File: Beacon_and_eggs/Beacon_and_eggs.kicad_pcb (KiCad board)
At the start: 2 copper layers, 47.7 x 65.9 mm, 42 parts, among them J1 USB_C_Receptacle_USB2.0_16P, Q1 IRLML0030, SW1 Boot, SW2 Reset, U1 SA818V, U2 STM32F411CEUx, U3 ADXL343, U6 MCP1253-33X50I/MS, U7 MCP1253-33X50I/MS, Y1 25MHz 18pF, Y2 32.768kHz 12.5pF

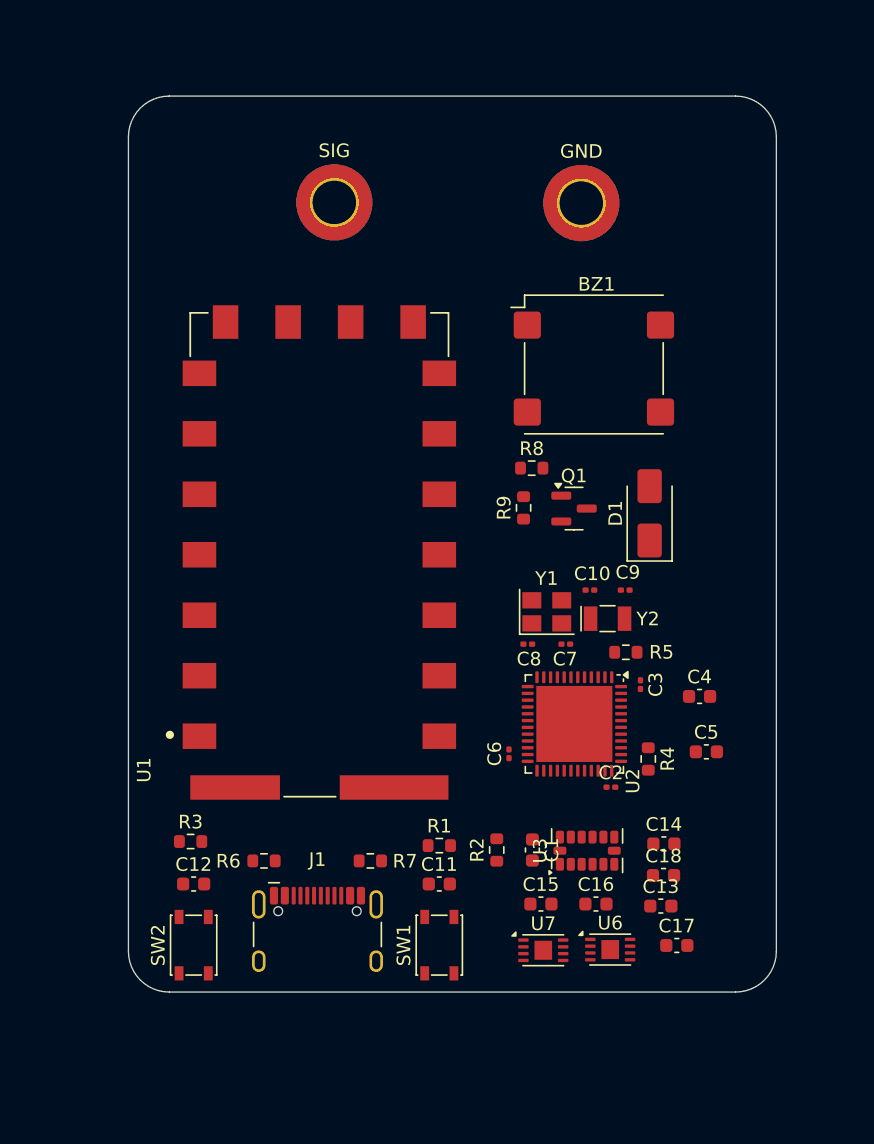
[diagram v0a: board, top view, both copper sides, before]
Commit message: Laid traces and changed 3.3V regulator
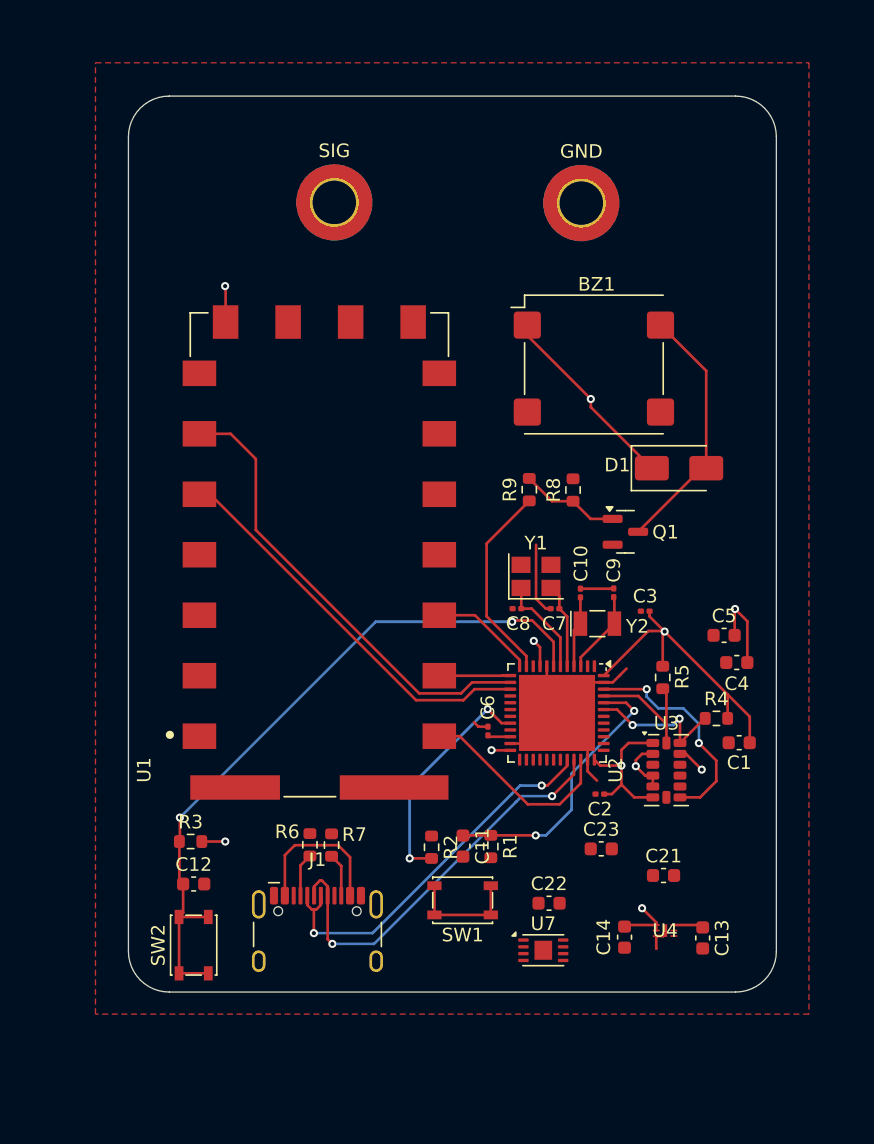
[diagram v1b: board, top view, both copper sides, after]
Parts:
- removed C15: 10uF, Capacitor_SMD:C_0603_1608Metric
- removed U6: MCP1253-33X50I/MS, Package_DFN_QFN:TDFN-8-1EP_3x2mm_P0.5mm_EP1.3x1.4mm
- added U4: MIC5528-3.3YMX-TR, footprints:XTDFN6_1P2X1P2_MCH, F.Cu at (156.9, 116.3)
- C14: value 1uF -> 2.2uF
- moved C1 17.1 mm to (162.4, 102.5), turned to 0 degrees
- moved C23 9.03 mm to (152.2, 110.3)
- moved C5 8.67 mm to (161.3, 94.6), turned to 180 degrees
- moved U3 8.32 mm to (157.0, 104.5), turned to 0 degrees
- moved C14 7.45 mm to (153.9, 116.8), turned to -90 degrees
- moved R4 5.84 mm to (160.7, 100.7), turned to 0 degrees
- moved C3 5.42 mm to (155.4, 92.8), turned to 180 degrees
- moved R2 4.80 mm to (139.7, 110.2), turned to -90 degrees
- moved Q1 4.15 mm to (154.0, 87.0)
- moved D1 3.96 mm to (157.9, 82.3), turned to 0 degrees
- moved C13 3.87 mm to (159.7, 116.9), turned to -90 degrees
- moved R1 3.79 mm to (144.1, 110.2), turned to -90 degrees
- moved SW1 3.72 mm to (142.0, 114.1), turned to 0 degrees
- moved C4 3.71 mm to (162.2, 96.6)
- moved R6 3.58 mm to (130.8, 110.0), turned to 90 degrees
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- renumbered C18 to C21, C16 to C22, C17 to C23
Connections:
- C14 pad 1: Net-(U6-C+) -> +3.3V
- C14 pad 2: Net-(U6-C-) -> GND
- J1 pad A4: +3.3V -> +5V
- J1 pad A9: +3.3V -> +5V
- J1 pad B4: +3.3V -> +5V
- J1 pad B9: +3.3V -> +5V
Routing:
- net +3.3V: track 0.00 -> 81.0 mm, vias 0 -> 10
- net NRST: track 0.00 -> 51.8 mm, vias 0 -> 2
- net GND: track 0.00 -> 36.1 mm, vias 0 -> 1
- net TX POWER DOWN: track 0.00 -> 34.2 mm
- net USB Dp: track 0.00 -> 30.4 mm, vias 0 -> 2
- net TX EN: track 0.00 -> 29.5 mm
- net USB Dn: track 0.00 -> 28.6 mm, vias 0 -> 2
- net BOOT0: track 0.00 -> 20.5 mm, vias 0 -> 2
- net Net-(BZ1--): track 0.00 -> 18.9 mm
- net BOOT1: track 0.00 -> 17.1 mm, vias 0 -> 2
- net ACCEL INT1: track 0.00 -> 16.3 mm, vias 0 -> 2
- net TX AUDIO SIGNAL: track 0.00 -> 14.9 mm
- net BUZZ: track 0.00 -> 14.7 mm
- net +5V: track 0.00 -> 11.3 mm
- net SDA: track 0.00 -> 10.7 mm, vias 0 -> 2
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- added copper zone on In1.Cu, net +3.3V
- added copper zone on F.Cu, net GND
- added copper zone on In2.Cu, net GND
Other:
- copper layers 2 -> 4

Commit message: cheanged schematic and V1 pcb layout completed.
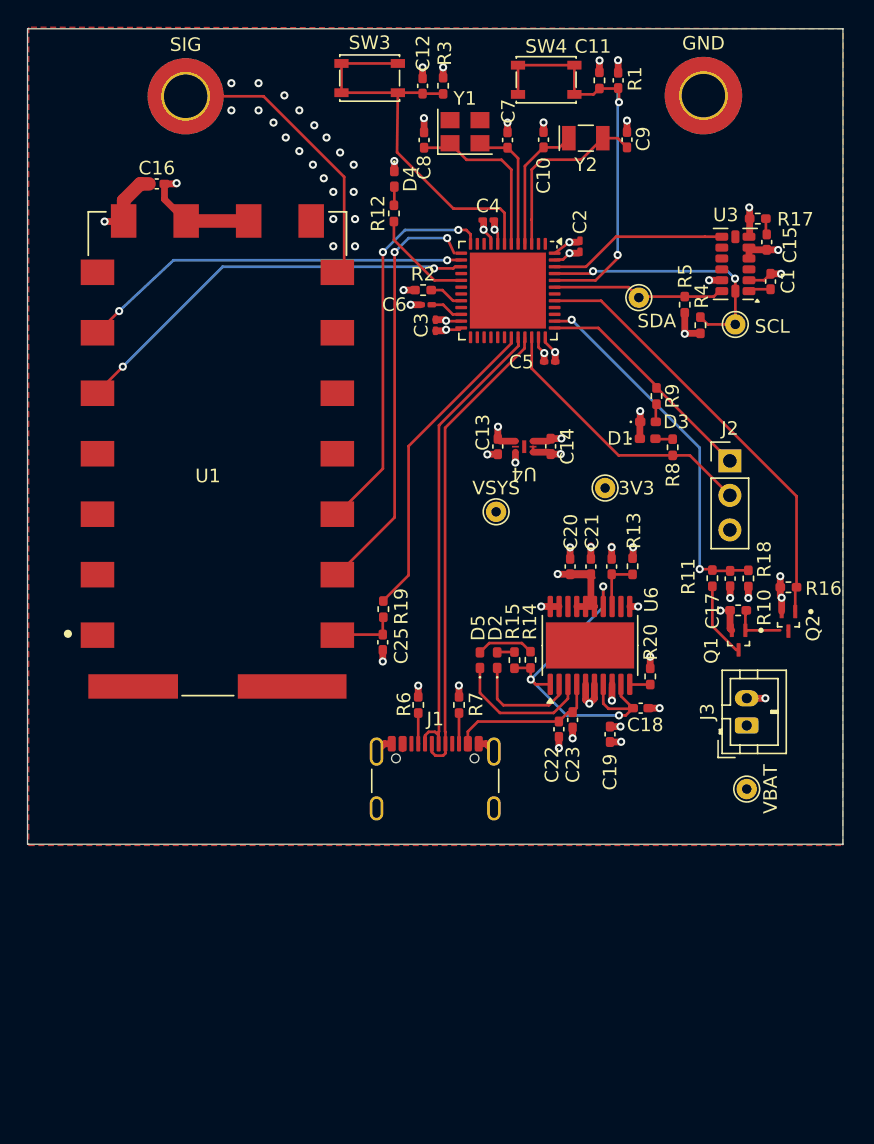
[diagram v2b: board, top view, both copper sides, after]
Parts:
- removed BZ1: Buzzer, Buzzer_Beeper:MagneticBuzzer_PUI_SMT-1028-T-2-R
- removed the GND at (150.8, 62.8)
- removed SW1: Boot, Button_Switch_SMD:SW_SPST_PTS810
- removed SW2: Reset, Button_Switch_SMD:SW_SPST_PTS810
- removed U7: MCP1253-33X50I/MS, Package_DFN_QFN:TDFN-8-1EP_3x2mm_P0.5mm_EP1.3x1.4mm
- added 3V3: 3V3, TestPoint:TestPoint_THTPad_D1.5mm_Drill0.7mm, F.Cu at (152.5, 83.8)
- added C15: 10uF, Capacitor_SMD:C_0402_1005Metric_Pad0.74x0.62mm_HandSolder, F.Cu at (164.4, 65.7)
- added C16: 0.1uF, Capacitor_SMD:C_0402_1005Metric_Pad0.74x0.62mm_HandSolder, F.Cu at (119.5, 61.4)
- added C17: 1nF, Capacitor_SMD:C_0402_1005Metric_Pad0.74x0.62mm_HandSolder, F.Cu at (161.7, 90.5)
- added C18: 0.1uF, Capacitor_SMD:C_0402_1005Metric_Pad0.74x0.62mm_HandSolder, F.Cu at (155.1, 100.0)
- added C19: 33uF, Capacitor_SMD:C_0402_1005Metric_Pad0.74x0.62mm_HandSolder, F.Cu at (152.9, 101.9)
- added C20: 0.1uF, Capacitor_SMD:C_0402_1005Metric_Pad0.74x0.62mm_HandSolder, F.Cu at (149.9, 89.6)
- added C24: 10nF, Capacitor_SMD:C_0402_1005Metric_Pad0.74x0.62mm_HandSolder, F.Cu at (153.0, 89.6)
- added C25: 33nF, Capacitor_SMD:C_0402_1005Metric_Pad0.74x0.62mm_HandSolder, F.Cu at (136.1, 95.1)
- added D2: RED LED, LED_SMD:LED_0402_1005Metric_Pad0.77x0.64mm_HandSolder, F.Cu at (144.6, 96.5)
- added D3: UCLAMP3311P.TCT, Diode_SMD:D_0402_1005Metric_Pad0.77x0.64mm_HandSolder, F.Cu at (155.7, 78.9)
- added D4: BLUE LED, LED_SMD:LED_0402_1005Metric_Pad0.77x0.64mm_HandSolder, F.Cu at (137.0, 61.0)
- added D5: GREEN LED, LED_SMD:LED_0402_1005Metric_Pad0.77x0.64mm_HandSolder, F.Cu at (143.3, 96.5)
- added GND: MountingHole_3.2mm_M3_ISO7380_Pad_TopBottom, MountingHole:MountingHole_3.2mm_M3_ISO7380_Pad_TopBottom, F.Cu at (159.7, 54.9)
- added J2: Conn_01x03_Pin, Connector_PinHeader_2.54mm:PinHeader_1x03_P2.54mm_Vertical, F.Cu at (161.7, 81.8)
- added J3: Conn_01x02_Pin, Connector_JST:JST_PH_B2B-PH-K_1x02_P2.00mm_Vertical, F.Cu at (162.9, 101.3)
- added Q2: NTA4153N, NTA4151PT1G:SOT50P160X90-3N, F.Cu at (166.0, 93.6)
- added R10: 51k, Resistor_SMD:R_0402_1005Metric_Pad0.72x0.64mm_HandSolder, F.Cu at (162.3, 92.8)
- added R11: 51k, Resistor_SMD:R_0402_1005Metric_Pad0.72x0.64mm_HandSolder, F.Cu at (160.4, 90.4)
- added R12: 250R, Resistor_SMD:R_0402_1005Metric_Pad0.72x0.64mm_HandSolder, F.Cu at (137.0, 63.6)
- added R13: 37.4K, Resistor_SMD:R_0402_1005Metric_Pad0.72x0.64mm_HandSolder, F.Cu at (154.5, 89.5)
- added R14: 1.5K, Resistor_SMD:R_0402_1005Metric_Pad0.72x0.64mm_HandSolder, F.Cu at (147.0, 96.4)
- added R15: 1.5K, Resistor_SMD:R_0402_1005Metric_Pad0.72x0.64mm_HandSolder, F.Cu at (145.8, 96.5)
- added R16: 510k, Resistor_SMD:R_0402_1005Metric_Pad0.72x0.64mm_HandSolder, F.Cu at (166.0, 91.1)
- added R17: 50R, Resistor_SMD:R_0402_1005Metric_Pad0.72x0.64mm_HandSolder, F.Cu at (163.7, 64.0)
- added R18: 51k, Resistor_SMD:R_0402_1005Metric_Pad0.72x0.64mm_HandSolder, F.Cu at (163.0, 90.4)
- added R19: 3.3K, Resistor_SMD:R_0402_1005Metric_Pad0.72x0.64mm_HandSolder, F.Cu at (136.2, 92.7)
- added R20: 1K, Resistor_SMD:R_0402_1005Metric_Pad0.72x0.64mm_HandSolder, F.Cu at (155.8, 97.7)
- added SW3: RESET, Button_Switch_SMD:SW_SPST_PTS810, F.Cu at (135.2, 53.6)
- added SW4: BOOT0, Button_Switch_SMD:SW_SPST_PTS810, F.Cu at (148.2, 53.8)
- added TP3: SCL, TestPoint:TestPoint_THTPad_D1.5mm_Drill0.7mm, F.Cu at (162.1, 71.8)
- added TP4: SDA, TestPoint:TestPoint_THTPad_D1.5mm_Drill0.7mm, F.Cu at (155.0, 69.8)
- added TP5: VBAT, TestPoint:TestPoint_THTPad_D1.5mm_Drill0.7mm, F.Cu at (162.9, 105.9)
- added TP6: VSYS, TestPoint:TestPoint_THTPad_D1.5mm_Drill0.7mm, F.Cu at (144.5, 85.5)
- added U6: BQ24070RHLR, Package_SO:HTSSOP-20-1EP_4.4x6.5mm_P0.65mm_EP3.4x6.5mm_Mask2.4x3.7mm, F.Cu at (151.4, 95.4)
- C1: value C -> 0.1F; footprint Capacitor_SMD:C_0603_1608Metric -> Capacitor_SMD:C_0402_1005Metric_Pad0.74x0.62mm_HandSolder
- C10, C7, C8, C9: footprint Capacitor_SMD:C_0201_0603Metric -> Capacitor_SMD:C_0402_1005Metric_Pad0.74x0.62mm_HandSolder
- C11, C12, C14, C21: footprint Capacitor_SMD:C_0603_1608Metric -> Capacitor_SMD:C_0402_1005Metric_Pad0.74x0.62mm_HandSolder
- C13: value 10uF -> 2.2uF; footprint Capacitor_SMD:C_0603_1608Metric -> Capacitor_SMD:C_0402_1005Metric_Pad0.74x0.62mm_HandSolder
- C2, C3, C6: footprint Capacitor_SMD:C_0201_0603Metric -> Capacitor_SMD:C_0201_0603Metric_Pad0.64x0.40mm_HandSolder
- C22: value 10uF -> 0.1uF; footprint Capacitor_SMD:C_0603_1608Metric -> Capacitor_SMD:C_0402_1005Metric_Pad0.74x0.62mm_HandSolder
- C23: value 1uF -> 10uF; footprint Capacitor_SMD:C_0603_1608Metric -> Capacitor_SMD:C_0402_1005Metric_Pad0.74x0.62mm_HandSolder
- C4, C5: footprint Capacitor_SMD:C_0603_1608Metric -> Capacitor_SMD:C_0201_0603Metric_Pad0.64x0.40mm_HandSolder
- D1: value SS14 -> UCLAMP3311P.TCT; footprint Diode_SMD:D_SMA -> Diode_SMD:D_0402_1005Metric_Pad0.77x0.64mm_HandSolder
- J1: footprint Connector_USB:USB_C_Receptacle_HCTL_HC-TYPE-C-16P-01A -> Connector_USB:USB_C_Receptacle_GCT_USB4105-xx-A_16P_TopMnt_Horizontal
- Q1: value IRLML0030 -> NTA4151P; footprint Package_TO_SOT_SMD:SOT-23 -> NTA4151PT1G:SOT50P160X90-3N
- R1, R2, R3, R4, R5, R6, R7: footprint Resistor_SMD:R_0603_1608Metric -> Resistor_SMD:R_0402_1005Metric_Pad0.72x0.64mm_HandSolder
- R8: value 100k -> 250R; footprint Resistor_SMD:R_0603_1608Metric -> Resistor_SMD:R_0402_1005Metric_Pad0.72x0.64mm_HandSolder
- R9: value 100 -> 250R; footprint Resistor_SMD:R_0603_1608Metric -> Resistor_SMD:R_0402_1005Metric_Pad0.72x0.64mm_HandSolder
- SIG: value MountingHole_3.2mm_M3_DIN965_Pad_TopBottom -> FABRIC_ANT_HOLES
- moved C12 61.1 mm to (139.1, 54.2), turned to 90 degrees
- moved R3 58.6 mm to (140.6, 54.2), turned to 90 degrees
- moved C11 57.5 mm to (153.5, 53.8), turned to 90 degrees
- moved R1 56.9 mm to (152.1, 53.8)
- moved R2 41.0 mm to (139.1, 69.2), turned to 0 degrees
- moved C2 40.3 mm to (150.7, 66.0), turned to 90 degrees
- moved C13 39.2 mm to (144.6, 80.7)
- moved U3 37.6 mm to (162.1, 67.3), turned to 180 degrees
- moved C4 37.3 mm to (143.9, 64.1), turned to 180 degrees
- moved U4 37.1 mm to (146.5, 80.7), turned to 180 degrees
- moved C14 36.5 mm to (148.5, 80.7), turned to 90 degrees
- moved Y2 35.7 mm to (151.1, 58.0)
- moved C8 35.2 mm to (139.2, 58.2), turned to -90 degrees
- moved C7 34.7 mm to (145.3, 58.2), turned to -90 degrees
- moved C1 34.0 mm to (164.7, 68.6), turned to 90 degrees
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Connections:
- net ACCEL INT1 renamed /ACCEL_INT1
- net BOOT1 renamed /BOOT1
- net NRST renamed /NRST
- net Net-(U2-PC14) renamed /X2_IN
- net Net-(U2-PC15) renamed /X2_OUT
- net Net-(U2-PH0) renamed /X1_IN
- net Net-(U2-PH1) renamed /X1_OUT
- net RXD renamed /RXD
- net TX EN renamed /TX_EN
- net TX POWER DOWN renamed /TX_PWR_DN
- net TXD renamed /TXD
- net USB Dn renamed /USB_DN
- net USB Dp renamed /USB_DP
- C1 pad 1: GND -> Net-(U3-Vdd_I/O)
- C1 pad 2: +3.3V -> GND
- C11 pad 1: BOOT0 -> /BOOT0
- C13 pad 1: +BATT -> VSYS
- C21 pad 1: +5V -> VSYS
- C22 pad 1: +3V3 -> VBUS
- C23 pad 1: Net-(U7-C+) -> VBUS
- C23 pad 2: Net-(U7-C-) -> GND
- D1 pad 1: +3.3V -> GND
- D1 pad 2: Net-(BZ1--) -> Net-(D1-A2)
- J1 pad A4: +5V -> VBUS
- J1 pad A9: +5V -> VBUS
- J1 pad B4: +5V -> VBUS
- J1 pad B9: +5V -> VBUS
- Q1 pad 1: Net-(Q1-G) -> Net-(Q1-G1)
- Q1 pad 2: GND -> VBAT
- Q1 pad 3: Net-(BZ1--) -> Net-(Q1-D1-Pad3)
- R1 pad 1: BOOT0 -> GND
- R1 pad 2: GND -> /BOOT0
- R4 pad 1: SDA -> /SCL
- R5 pad 1: SCL -> /SDA
- R8 pad 1: Net-(Q1-G) -> Net-(D1-A2)
- R8 pad 2: GND -> /SWDIO
- R9 pad 1: BUZZ -> /SWCLK
- R9 pad 2: Net-(Q1-G) -> Net-(D3-A2)
- SIG pad 1: (no net) -> /ANT_SIG
- U1 pad 12: RF_IN -> /ANT_SIG
- U1 pad 18: TX AUDIO SIGNAL -> Net-(U1-MIC_IN)
- U1 pad 8: +3.3V -> VSYS
- U2 pad 11: BUZZ -> unconnected-(U2-PA1-Pad11)
- U2 pad 17: unconnected-(U2-PA7-Pad17) -> /LED1
- U2 pad 29: REG_SHDN -> unconnected-(U2-PA8-Pad29)
- U2 pad 31: unconnected-(U2-PA10-Pad31) -> /TX_AUDIO_SIGNAL
- U2 pad 34: TX AUDIO SIGNAL -> /SWDIO
- U2 pad 37: unconnected-(U2-PA14-Pad37) -> /SWCLK
- U2 pad 38: unconnected-(U2-PA15-Pad38) -> /BATT_V_ADC
- U2 pad 41: unconnected-(U2-PB5-Pad41) -> /BATT_EN
- U2 pad 43: SDA -> /SDA
- U2 pad 44: BOOT0 -> /BOOT0
- U2 pad 45: SCL -> /SCL
- U3 pad 1: +3.3V -> Net-(U3-Vdd_I/O)
- U3 pad 13: SDA -> /SDA
- U3 pad 14: SCL -> /SCL
- U4 pad 4: unconnected-(U4-EN-Pad4) -> VSYS
- U4 pad 6: +BATT -> VSYS
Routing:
- net +3.3V: track 81.0 -> 17.4 mm, vias 10 -> 9
- net /BATT_EN: track 0.00 -> 32.4 mm
- net /BOOT0: track 0.00 -> 30.9 mm, vias 0 -> 2
- net /VREF: track 0.00 -> 28.9 mm, vias 0 -> 3
- net /BATT_V_ADC: track 0.00 -> 27.2 mm, vias 0 -> 2
- net /TXD: track 6.36 -> 31.0 mm, vias 0 -> 2
- net /TX_AUDIO_SIGNAL: track 0.00 -> 23.3 mm
- net GND: track 36.1 -> 58.3 mm, vias 1 -> 60
- net /ANT_SIG: track 0.00 -> 21.3 mm
- net /NRST: track 51.8 -> 30.5 mm, vias 2 -> 0
- net /SWDIO: track 0.00 -> 21.1 mm
- net /RXD: track 7.74 -> 28.6 mm, vias 0 -> 2
- net BOOT0: track 20.5 -> 0.00 mm, vias 2 -> 0
- net /SCL: track 0.00 -> 19.7 mm, vias 0 -> 2
- net Net-(BZ1--): track 18.9 -> 0.00 mm
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- added copper zone on In2.Cu, net +3.3V
- added copper zone on In1.Cu, net GND
- added copper zone on In2.Cu, net VBAT
- added copper zone on In2.Cu, net VSYS
- removed copper zone on In1.Cu, net +3.3V
- removed copper zone on In2.Cu, net GND
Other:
- board size 47.7 x 65.9 mm -> 60 x 60 mm

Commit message: narrowed the pcb down from 60mm to 40 mm
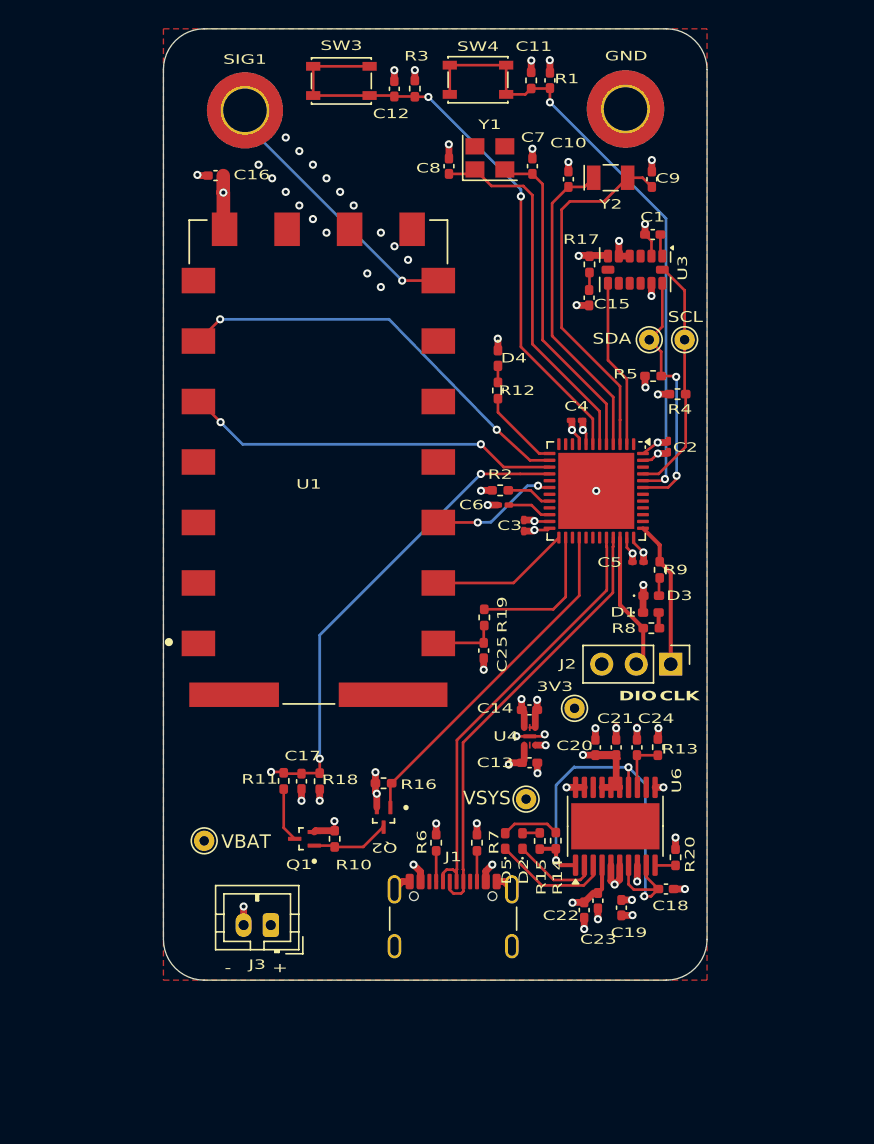
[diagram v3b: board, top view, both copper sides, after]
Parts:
- moved TP5 40.1 mm to (123.0, 109.8)
- moved J3 38.0 mm to (127.9, 116.0), turned to 180 degrees
- moved Q1 35.1 mm to (130.4, 109.6), turned to 180 degrees
- moved C17 34.9 mm to (130.2, 105.4)
- moved R11 34.9 mm to (128.8, 105.3)
- moved R18 34.9 mm to (131.5, 105.4)
- moved R10 34.1 mm to (132.6, 109.6), turned to 90 degrees
- moved Q2 33.1 mm to (136.2, 108.0)
- moved R16 33.1 mm to (136.2, 105.5)
- moved C13 23.4 mm to (146.9, 104.0), turned to 0 degrees
- moved U4 21.3 mm to (147.0, 102.1), turned to -90 degrees
- moved TP6 21.3 mm to (146.7, 106.7)
- moved C14 19.5 mm to (146.9, 100.1), turned to 180 degrees
- moved 3V3 16.4 mm to (150.2, 100.0)
- moved C2 16.1 mm to (157.2, 80.7)
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- renumbered SIG to SIG1
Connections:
- U2 pad 12: /RXD -> unconnected-(U2-PA2-Pad12)
- U2 pad 13: /TXD -> /LED1
- U2 pad 16: unconnected-(U2-PA6-Pad16) -> /BATT_V_ADC
- U2 pad 17: /LED1 -> unconnected-(U2-PA7-Pad17)
- U2 pad 18: unconnected-(U2-PB0-Pad18) -> /RXD
- U2 pad 2: unconnected-(U2-PC13-Pad2) -> /ACCEL_INT1
- U2 pad 25: unconnected-(U2-PB12-Pad25) -> /TXD
- U2 pad 26: unconnected-(U2-PB13-Pad26) -> /TX_AUDIO_SIGNAL
- U2 pad 28: unconnected-(U2-PB15-Pad28) -> /BATT_EN
- U2 pad 31: /TX_AUDIO_SIGNAL -> unconnected-(U2-PA10-Pad31)
- U2 pad 38: /BATT_V_ADC -> unconnected-(U2-PA15-Pad38)
- U2 pad 41: /BATT_EN -> unconnected-(U2-PB5-Pad41)
- U2 pad 46: /ACCEL_INT1 -> unconnected-(U2-PB9-Pad46)
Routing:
- net /TXD: track 31.0 -> 10.3 mm, vias 2 -> 0
- net /RXD: track 28.6 -> 9.48 mm
- net /NRST: track 30.5 -> 45.9 mm, vias 0 -> 2
- net /BOOT0: track 30.9 -> 46.1 mm
- net /X1_IN: track 9.56 -> 24.3 mm
- net /X1_OUT: track 12.8 -> 27.4 mm
- net /X2_OUT: track 9.81 -> 23.4 mm
- net /X2_IN: track 13.7 -> 26.9 mm
- net /TX_AUDIO_SIGNAL: track 23.3 -> 10.8 mm
- net /SWDIO: track 21.1 -> 10.2 mm
- net /BATT_V_ADC: track 27.2 -> 35.7 mm, vias 2 -> 3
- net /BATT_EN: track 32.4 -> 25.6 mm
- net /SDA: track 12.9 -> 19.1 mm, vias 0 -> 2
- net /SWCLK: track 17.0 -> 11.0 mm
- net GND: track 58.3 -> 52.6 mm, vias 60 -> 44
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- added copper zone on In2.Cu, net VBUS
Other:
- board size 60 x 60 mm -> 40 x 70 mm
- board text added: "+"
- board text added: "-"
- board text added: "CLK"
- board text added: "DIO"
